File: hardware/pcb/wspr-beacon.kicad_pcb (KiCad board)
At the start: 2 copper layers, 100 x 70 mm, 79 parts, among them J1 USB_OTG, J2 Conn_01x04, J3 Conn_02x03_Odd_Even, J4 Conn_Coaxial, J5 Conn_Coaxial, J6 Conn_Coaxial, SW1 SW_Push, U1 AP1117-33, U2 ATMEGA328-AU, U3 Si5351A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

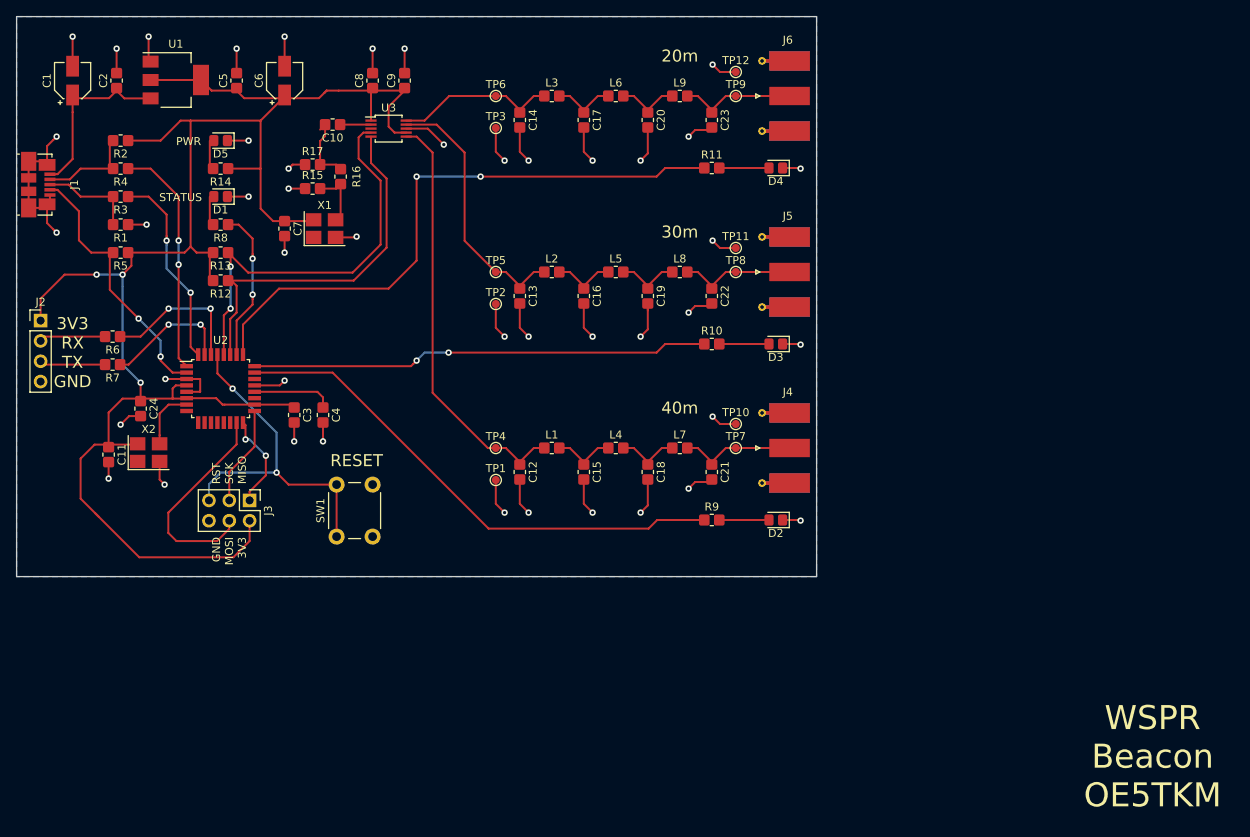
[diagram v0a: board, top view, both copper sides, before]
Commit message: Increase trace width for power and RF lines
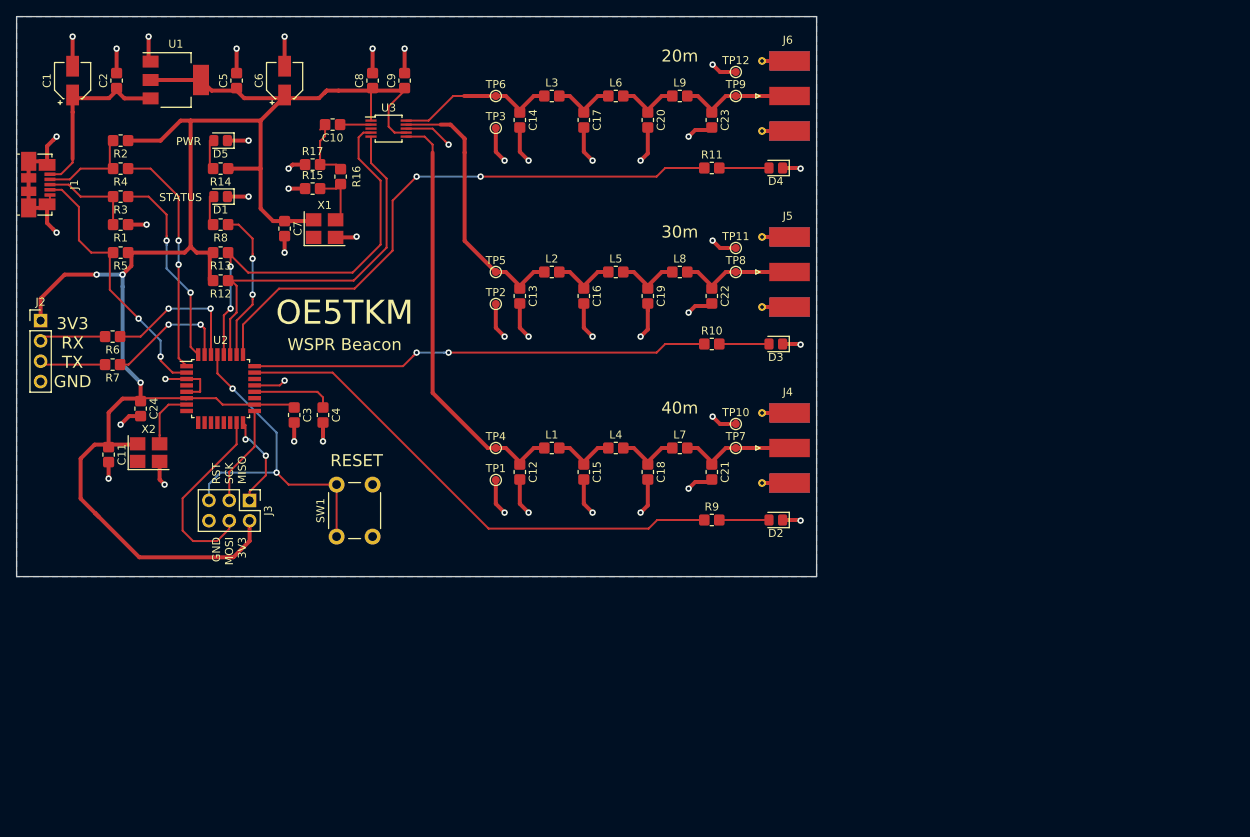
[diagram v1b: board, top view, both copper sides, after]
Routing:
- net /MOSI: track 27.0 -> 24.3 mm
- net /LED_40M: track 75.3 -> 72.8 mm
- net +3V3: track 225.9 -> 223.4 mm
- net Net-(C13-Pad1): track 32.4 -> 33.4 mm
- net GND: track 184.2 -> 184.8 mm
- net Net-(C12-Pad1): track 52.1 -> 52.7 mm
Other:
- board text added: "OE5TKM"
- board text added: "WSPR Beacon"
- board text removed: "WSPR Beacon OE5TKM"
